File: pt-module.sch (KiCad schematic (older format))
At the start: 6 parts, among them J1 M12 in, J2 Ethercon out, J3 PWR in, J4 M12 out, J5 Ethercon out, SW1 pwr-source switch

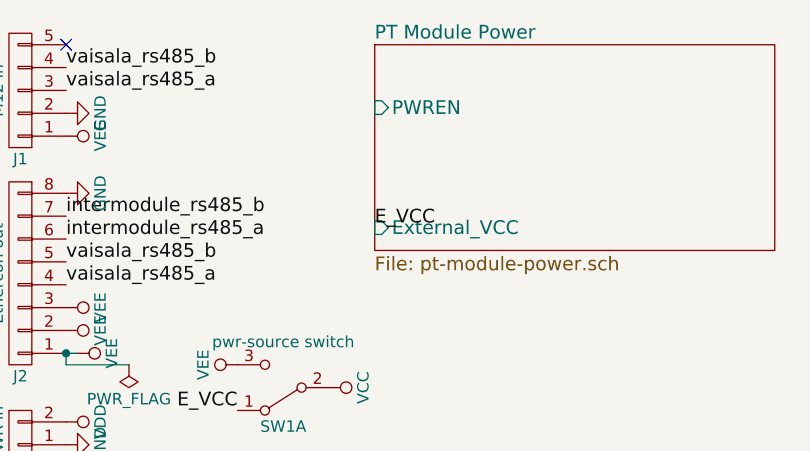
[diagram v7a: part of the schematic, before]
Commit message: Delete pwren
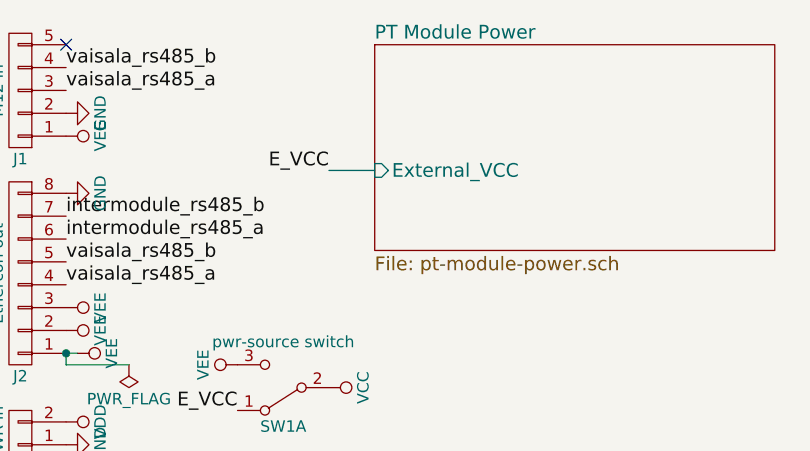
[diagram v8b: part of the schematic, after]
